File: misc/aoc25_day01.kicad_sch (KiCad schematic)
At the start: 13 parts, among them U1 74AHC541, U2 ATtiny85-20P, U3 25LC1024

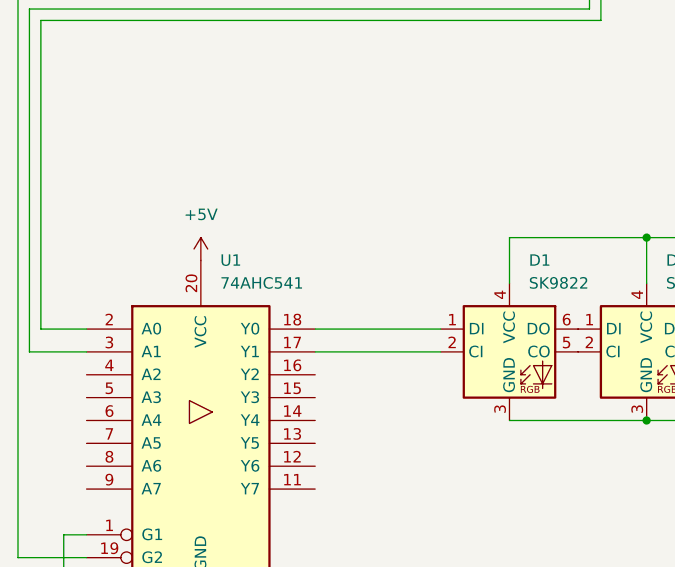
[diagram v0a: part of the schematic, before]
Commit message: fix incorrect comment in the memory defs file, fix incorrect value in the schematic
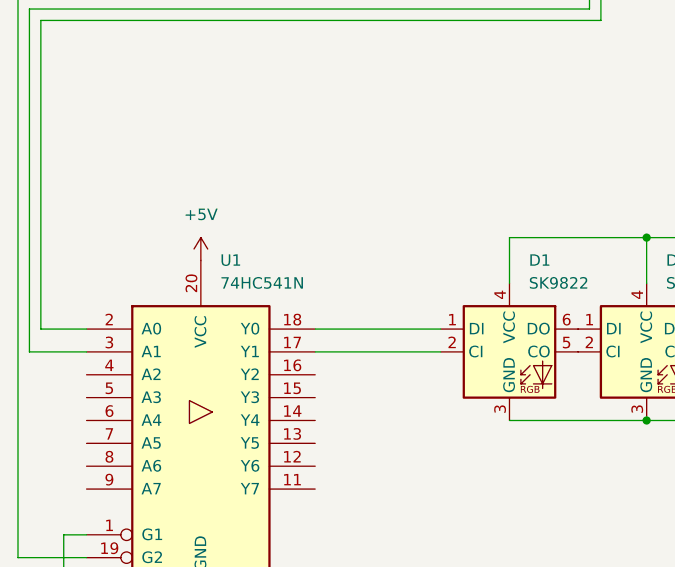
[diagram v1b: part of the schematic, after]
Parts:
- U1: value 74AHC541 -> 74HC541N
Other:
- company: (none) -> github.com/hawaite
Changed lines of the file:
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@@
 	(title_block
 		(title "ATTiny85 Advent of Code Thing")
+		(rev "a")
+		(company "github.com/hawaite")
 	)
 	(text "CE_LEDS"
@@
 			)
 		)
-		(property "Value" "74AHC541"
+		(property "Value" "74HC541N"
 			(at 68.1833 130.81 0)
 			(effects
